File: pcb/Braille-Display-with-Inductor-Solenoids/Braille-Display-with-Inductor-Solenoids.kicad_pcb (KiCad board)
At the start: 2 copper layers, 58.2 x 57.4 mm, 60 parts, among them J1 Screw_Terminal_01x02, J2 Screw_Terminal_01x02, J3 Screw_Terminal_01x02, SW1 SW_Push, SW2 SW_Push, U1 RP2040-Zero, U2 TPIC6595, U3 TPIC6595, U4 TPIC6595

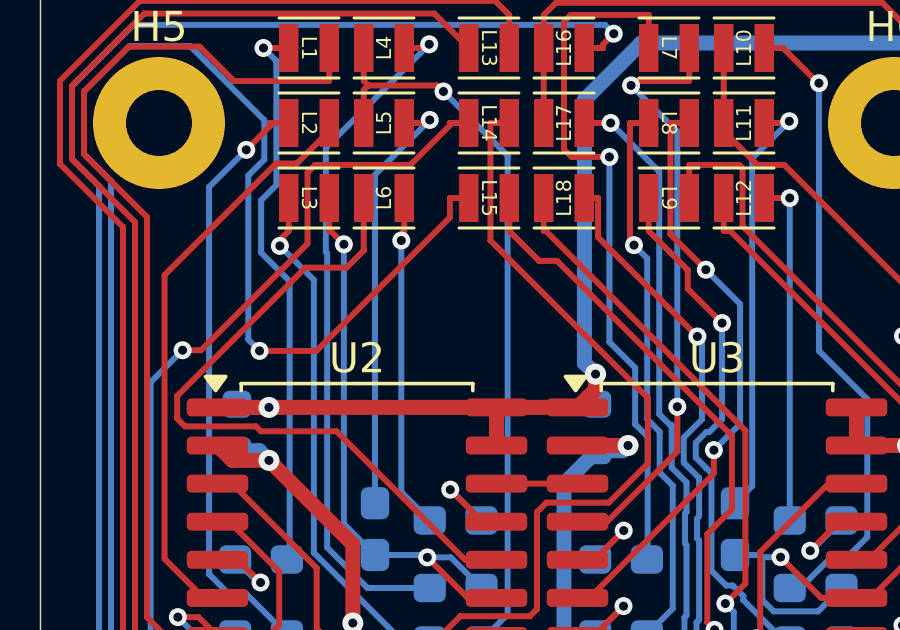
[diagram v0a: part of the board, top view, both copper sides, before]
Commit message: Create rev1_flat production files
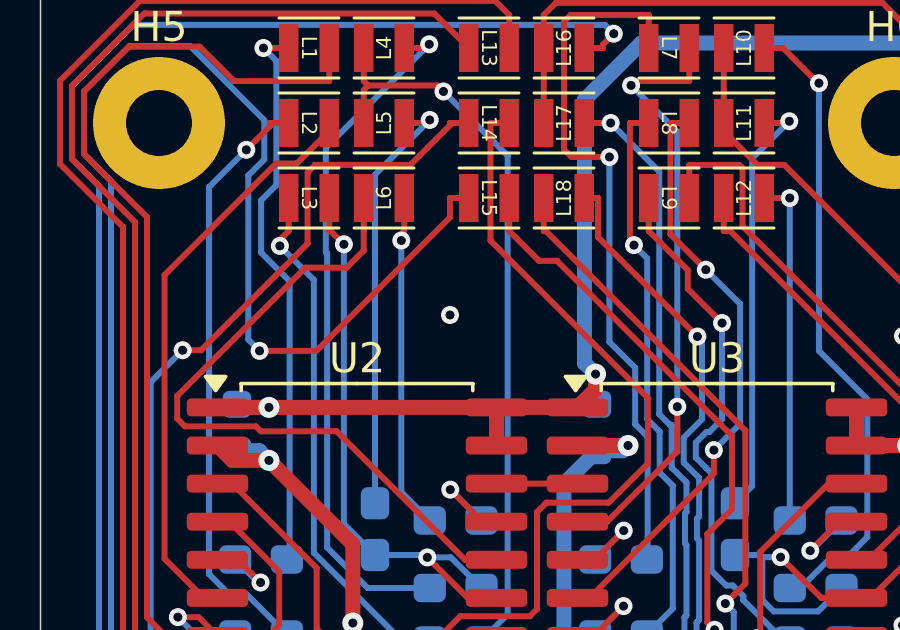
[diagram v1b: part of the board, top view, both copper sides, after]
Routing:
- net GND: vias 18 -> 19
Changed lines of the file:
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@@
+	)
+	(via
+		(at 104.7 108.9)
+		(size 0.6)
+		(drill 0.3)
+		(layers "F.Cu" "B.Cu")
+		(free yes)
+		(net 1)
 	)
 	(via
